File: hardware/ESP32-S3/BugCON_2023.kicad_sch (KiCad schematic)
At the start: 32 parts, among them J1 Conn_01x04_Pin, J2 Conn_01x04_Pin, J3 Conn_01x02, J4 Conn_01x01_Pin, J5 Conn_01x01_Pin, P1 USB_C_Plug_USB2.0, Q1 DMG3415U-7, SW1 RESET, SW2 GPIO, SW3 ON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

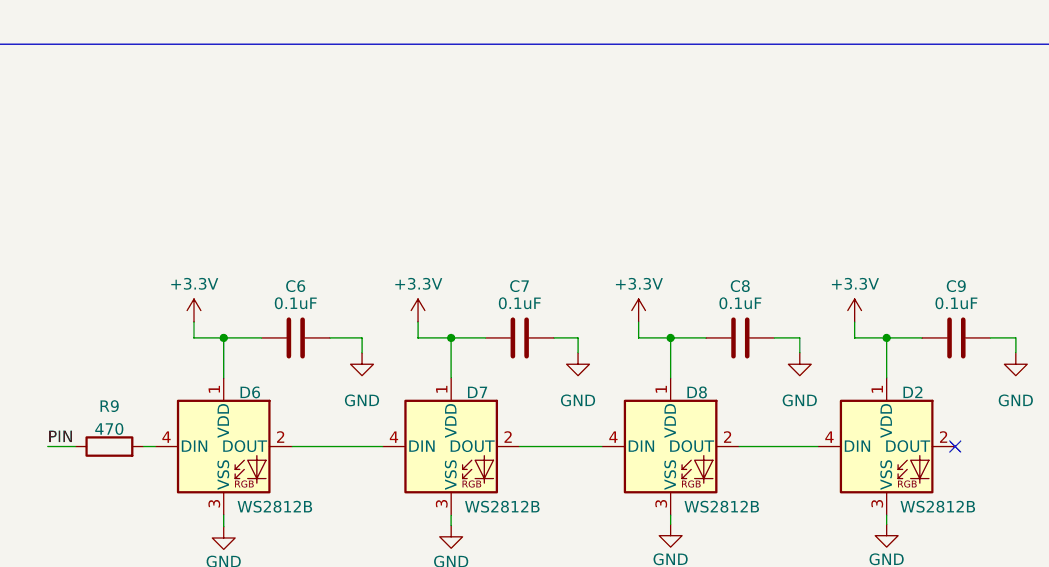
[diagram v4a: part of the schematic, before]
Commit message: fix 3.3v label on esp32 badge
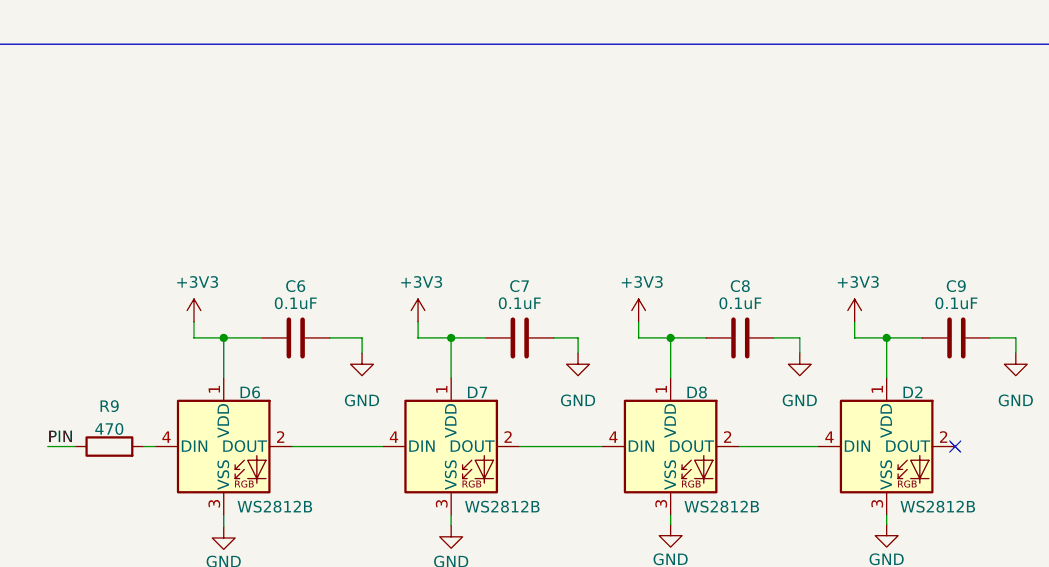
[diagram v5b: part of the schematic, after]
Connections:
- net +3.3V is gone; now on net +3V3: C6.2, C7.2, C8.2, C9.2, D2.1 (VDD), D6.1 (VDD), D7.1 (VDD), D8.1 (VDD)
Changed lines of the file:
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@@
     (effects (font (size 1.27 1.27)) (justify left bottom))
-  )
-  (symbol (lib_id "power:+3.3V") (at 231.394 121.666 0) (unit 1)
-    (in_bom yes) (on_board yes) (dnp no) (fields_autoplaced)
-    (property "Reference" "#PWR039" (at 231.394 125.476 0)
-      (effects (font (size 1.27 1.27)) hide)
-    )
-    (property "Value" "+3.3V" (at 231.394 117.475 0)
-      (effects (font (size 1.27 1.27)))
-    )
-    (property "Footprint" "" (at 231.394 121.666 0)
-      (effects (font (size 1.27 1.27)) hide)
-    )
-    (property "Datasheet" "" (at 231.394 121.666 0)
-      (effects (font (size 1.27 1.27)) hide)
-    )
-    (pin "1")
-    (instances
-      (project "BugCON_2023"
-        (path "/3bd1d1f8-54bc-46fd-8763-4ee40cf8320e"
-          (reference "#PWR039") (unit 1)
-        )
-      )
-      (project "ekoparty2023"
-        (path "/7698cad5-62ba-4b78-a0b3-4b9e419fd18c"
-          (reference "#PWR029") (unit 1)
-        )
-      )
-    )
-  )
-  (symbol (lib_id "power:+3.3V") (at 206.883 121.666 0) (unit 1)
-    (in_bom yes) (on_board yes) (dnp no) (fields_autoplaced)
-    (property "Reference" "#PWR036" (at 206.883 125.476 0)
-      (effects (font (size 1.27 1.27)) hide)
-    )
-    (property "Value" "+3.3V" (at 206.883 117.475 0)
-      (effects (font (size 1.27 1.27)))
-    )
-    (property "Footprint" "" (at 206.883 121.666 0)
-      (effects (font (size 1.27 1.27)) hide)
-    )
-    (property "Datasheet" "" (at 206.883 121.666 0)
-      (effects (font (size 1.27 1.27)) hide)
-    )
-    (pin "1")
-    (instances
-      (project "BugCON_2023"
-        (path "/3bd1d1f8-54bc-46fd-8763-4ee40cf8320e"
-          (reference "#PWR036") (unit 1)
-        )
-      )
-      (project "ekoparty2023"
-        (path "/7698cad5-62ba-4b78-a0b3-4b9e419fd18c"
-          (reference "#PWR028") (unit 1)
-        )
-      )
-    )
   )
   (symbol (lib_id "Device:C_Small") (at 106.426 37.973 0) (unit 1)
@@
     )
   )
+  (symbol (lib_id "power:+3V3") (at 206.883 121.666 0) (unit 1)
+    (in_bom yes) (on_board yes) (dnp no)
+    (property "Reference" "#PWR029" (at 206.883 125.476 0)
+      (effects (font (size 1.27 1.27)) hide)
+    )
+    (property "Value" "+3V3" (at 207.264 117.2718 0)
+      (effects (font (size 1.27 1.27)))
+    )
+    (property "Footprint" "" (at 206.883 121.666 0)
+      (effects (font (size 1.27 1.27)) hide)
+    )
+    (property "Datasheet" "" (at 206.883 121.666 0)
+      (effects (font (size 1.27 1.27)) hide)
+    )
+    (pin "1")
+    (instances
+      (project "BugCON_2023"
+        (path "/3bd1d1f8-54bc-46fd-8763-4ee40cf8320e"
+          (reference "#PWR029") (unit 1)
+        )
+      )
+      (project "minino"
+        (path "/aed8b10b-62ba-47cf-bd6c-c207f8432caa"
+          (reference "#PWR022") (unit 1)
+        )
+      )
+    )
+  )
   (symbol (lib_id "power:GND") (at 89.027 112.395 0) (unit 1)
     (in_bom yes) (on_board yes) (dnp no)
@@
     )
   )
+  (symbol (lib_id "power:+3V3") (at 255.397 121.666 0) (unit 1)
+    (in_bom yes) (on_board yes) (dnp no)
+    (property "Reference" "#PWR036" (at 255.397 125.476 0)
+      (effects (font (size 1.27 1.27)) hide)
+    )
+    (property "Value" "+3V3" (at 255.778 117.2718 0)
+      (effects (font (size 1.27 1.27)))
+    )
+    (property "Footprint" "" (at 255.397 121.666 0)
+      (effects (font (size 1.27 1.27)) hide)
+    )
+    (property "Datasheet" "" (at 255.397 121.666 0)
+      (effects (font (size 1.27 1.27)) hide)
+    )
+    (pin "1")
+    (instances
+      (project "BugCON_2023"
+        (path "/3bd1d1f8-54bc-46fd-8763-4ee40cf8320e"
+          (reference "#PWR036") (unit 1)
+        )
+      )
+      (project "minino"
+        (path "/aed8b10b-62ba-47cf-bd6c-c207f8432caa"
+          (reference "#PWR022") (unit 1)
+        )
+      )
+    )
+  )
   (symbol (lib_id "Connector:Conn_01x04_Pin") (at 24.384 116.967 0) (unit 1)
     (in_bom yes) (on_board yes) (dnp no) (fields_autoplaced)
@@
     )
   )
+  (symbol (lib_id "power:+3V3") (at 181.991 121.666 0) (unit 1)
+    (in_bom yes) (on_board yes) (dnp no)
+    (property "Reference" "#PWR032" (at 181.991 125.476 0)
+      (effects (font (size 1.27 1.27)) hide)
+    )
+    (property "Value" "+3V3" (at 182.372 117.2718 0)
+      (effects (font (size 1.27 1.27)))
+    )
+    (property "Footprint" "" (at 181.991 121.666 0)
+      (effects (font (size 1.27 1.27)) hide)
+    )
+    (property "Datasheet" "" (at 181.991 121.666 0)
+      (effects (font (size 1.27 1.27)) hide)
+    )
+    (pin "1")
+    (instances
+      (project "BugCON_2023"
+        (path "/3bd1d1f8-54bc-46fd-8763-4ee40cf8320e"
+          (reference "#PWR032") (unit 1)
+        )
+      )
+      (project "minino"
+        (path "/aed8b10b-62ba-47cf-bd6c-c207f8432caa"
+          (reference "#PWR022") (unit 1)
+        )
+      )
+    )
+  )
   (symbol (lib_id "Device:Fuse_Small") (at 47.752 21.336 0) (unit 1)
     (in_bom yes) (on_board yes) (dnp no)
@@
     )
   )
-  (symbol (lib_id "power:+3.3V") (at 181.991 121.666 0) (unit 1)
-    (in_bom yes) (on_board yes) (dnp no) (fields_autoplaced)
-    (property "Reference" "#PWR033" (at 181.991 125.476 0)
-      (effects (font (size 1.27 1.27)) hide)
-    )
-    (property "Value" "+3.3V" (at 181.991 117.475 0)
-      (effects (font (size 1.27 1.27)))
-    )
-    (property "Footprint" "" (at 181.991 121.666 0)
-      (effects (font (size 1.27 1.27)) hide)
-    )
-    (property "Datasheet" "" (at 181.991 121.666 0)
-      (effects (font (size 1.27 1.27)) hide)
-    )
-    (pin "1")
-    (instances
-      (project "BugCON_2023"
-        (path "/3bd1d1f8-54bc-46fd-8763-4ee40cf8320e"
-          (reference "#PWR033") (unit 1)
-        )
-      )
-      (project "ekoparty2023"
-        (path "/7698cad5-62ba-4b78-a0b3-4b9e419fd18c"
-          (reference "#PWR027") (unit 1)
-        )
-      )
-    )
-  )
   (symbol (lib_id "Connector_Generic:Conn_01x02") (at 38.1 85.598 0) (unit 1)
     (in_bom yes) (on_board yes) (dnp no)
@@
     )
   )
-  (symbol (lib_id "power:+3.3V") (at 255.397 121.666 0) (unit 1)
-    (in_bom yes) (on_board yes) (dnp no) (fields_autoplaced)
-    (property "Reference" "#PWR029" (at 255.397 125.476 0)
-      (effects (font (size 1.27 1.27)) hide)
-    )
-    (property "Value" "+3.3V" (at 255.397 117.475 0)
-      (effects (font (size 1.27 1.27)))
-    )
-    (property "Footprint" "" (at 255.397 121.666 0)
-      (effects (font (size 1.27 1.27)) hide)
-    )
-    (property "Datasheet" "" (at 255.397 121.666 0)
-      (effects (font (size 1.27 1.27)) hide)
-    )
-    (pin "1")
-    (instances
-      (project "BugCON_2023"
-        (path "/3bd1d1f8-54bc-46fd-8763-4ee40cf8320e"
-          (reference "#PWR029") (unit 1)
-        )
-      )
-      (project "ekoparty2023"
-        (path "/7698cad5-62ba-4b78-a0b3-4b9e419fd18c"
-          (reference "#PWR029") (unit 1)
-        )
-      )
-    )
-  )
   (symbol (lib_id "power:GND") (at 30.099 90.043 0) (unit 1)
     (in_bom yes) (on_board yes) (dnp no) (fields_autoplaced)
@@
         )
       )
+    )
+  )
+  (symbol (lib_id "power:+3V3") (at 231.394 121.666 0) (unit 1)
+    (in_bom yes) (on_board yes) (dnp no)
+    (property "Reference" "#PWR033" (at 231.394 125.476 0)
+      (effects (font (size 1.27 1.27)) hide)
+    )
+    (property "Value" "+3V3" (at 231.775 117.2718 0)
+      (effects (font (size 1.27 1.27)))
+    )
+    (property "Footprint" "" (at 231.394 121.666 0)
+      (effects (font (size 1.27 1.27)) hide)
+    )
+    (property "Datasheet" "" (at 231.394 121.666 0)
+      (effects (font (size 1.27 1.27)) hide)
+    )
+    (pin "1")
+    (instances
+      (project "BugCON_2023"
+        (path "/3bd1d1f8-54bc-46fd-8763-4ee40cf8320e"
+          (reference "#PWR033") (unit 1)
+        )
+      )
+      (project "minino"
+        (path "/aed8b10b-62ba-47cf-bd6c-c207f8432caa"
+          (reference "#PWR022") (unit 1)
+        )
+      )

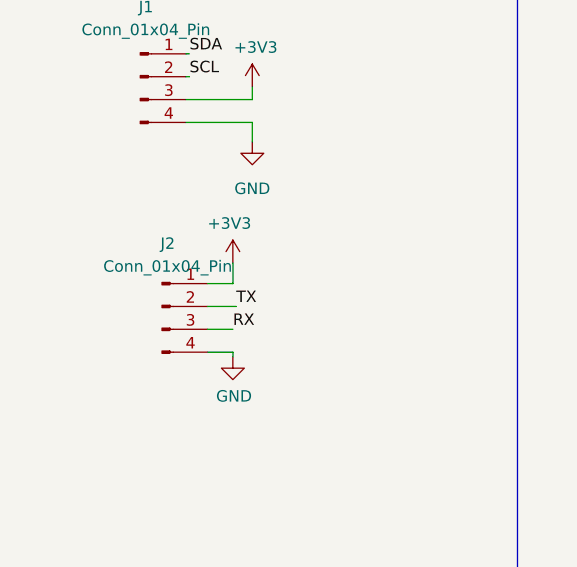
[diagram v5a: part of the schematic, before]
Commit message: remove 3.3v on Serial connector on esp32s3
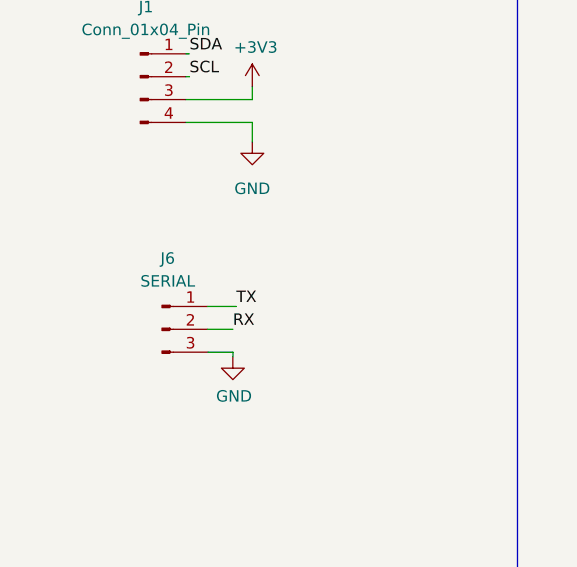
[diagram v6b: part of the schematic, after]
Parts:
- removed J2: Conn_01x04_Pin, Connector_PinSocket_2.54mm:PinSocket_1x04_P2.54mm_Vertical, symbol Connector:Conn_01x04_Pin
- added J6: SERIAL, Connector_PinSocket_2.54mm:PinSocket_1x03_P2.54mm_Vertical, symbol Connector:Conn_01x03_Pin
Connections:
- net GND: now also J6.3 (Pin_3)
- net RX: now also J6.2 (Pin_2)
- net TX: now also J6.1 (Pin_1)
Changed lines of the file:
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@@
-    (stroke (width 0) (type default))
-  )
-  (wire (pts (xy 34.671 137.668) (xy 34.671 139.954))
     (stroke (width 0) (type default))
   )
@@
   )
   (wire (pts (xy 154.305 35.052) (xy 156.337 35.052))
-    (stroke (width 0) (type default))
-  )
-  (wire (pts (xy 34.671 139.954) (xy 31.877 139.954))
     (stroke (width 0) (type default))
   )
@@
     )
   )
+  (symbol (lib_id "Connector:Conn_01x03_Pin") (at 26.797 145.034 0) (unit 1)
+    (in_bom yes) (on_board yes) (dnp no) (fields_autoplaced)
+    (property "Reference" "J6" (at 27.432 137.16 0)
+      (effects (font (size 1.27 1.27)))
+    )
+    (property "Value" "SERIAL" (at 27.432 139.7 0)
+      (effects (font (size 1.27 1.27)))
+    )
+    (property "Footprint" "Connector_PinSocket_2.54mm:PinSocket_1x03_P2.54mm_Vertical" (at 26.797 145.034 0)
+      (effects (font (size 1.27 1.27)) hide)
+    )
+    (property "Datasheet" "~" (at 26.797 145.034 0)
+      (effects (font (size 1.27 1.27)) hide)
+    )
+    (pin "1")
+    (pin "2")
+    (pin "3")
+    (instances
+      (project "BugCON_2023"
+        (path "/3bd1d1f8-54bc-46fd-8763-4ee40cf8320e"
+          (reference "J6") (unit 1)
+        )
+      )
+    )
+  )
   (symbol (lib_id "power:+3V3") (at 133.604 32.004 0) (unit 1)
     (in_bom yes) (on_board yes) (dnp no)
@@
         (path "/aed8b10b-62ba-47cf-bd6c-c207f8432caa"
           (reference "#PWR06") (unit 1)
-        )
-      )
-    )
-  )
-  (symbol (lib_id "Connector:Conn_01x04_Pin") (at 26.797 142.494 0) (unit 1)
-    (in_bom yes) (on_board yes) (dnp no) (fields_autoplaced)
-    (property "Reference" "J2" (at 27.432 135.509 0)
-      (effects (font (size 1.27 1.27)))
-    )
-    (property "Value" "Conn_01x04_Pin" (at 27.432 138.049 0)
-      (effects (font (size 1.27 1.27)))
-    )
-    (property "Footprint" "Connector_PinSocket_2.54mm:PinSocket_1x04_P2.54mm_Vertical" (at 26.797 142.494 0)
-      (effects (font (size 1.27 1.27)) hide)
-    )
-    (property "Datasheet" "~" (at 26.797 142.494 0)
-      (effects (font (size 1.27 1.27)) hide)
-    )
-    (property "Proveedor" "-- mixed values --" (at 26.797 142.494 0)
-      (effects (font (size 1.27 1.27)) hide)
-    )
-    (pin "1")
-    (pin "2")
-    (pin "3")
-    (pin "4")
-    (instances
-      (project "BugCON_2023"
-        (path "/3bd1d1f8-54bc-46fd-8763-4ee40cf8320e"
-          (reference "J2") (unit 1)
         )
       )
@@
         )
       )
-    )
-  )
-  (symbol (lib_id "power:+3V3") (at 34.671 137.668 0) (mirror y) (unit 1)
-    (in_bom yes) (on_board yes) (dnp no)
-    (property "Reference" "#PWR015" (at 34.671 141.478 0)
-      (effects (font (size 1.27 1.27)) hide)
-    )
-    (property "Value" "+3V3" (at 34.29 133.2738 0)
-      (effects (font (size 1.27 1.27)))
-    )
-    (property "Footprint" "" (at 34.671 137.668 0)
-      (effects (font (size 1.27 1.27)) hide)
-    )
-    (property "Datasheet" "" (at 34.671 137.668 0)
-      (effects (font (size 1.27 1.27)) hide)
-    )
-    (pin "1")
-    (instances
-      (project "BugCON_2023"
-        (path "/3bd1d1f8-54bc-46fd-8763-4ee40cf8320e"
-          (reference "#PWR015") (unit 1)
-        )
-      )
-      (project "minino"
-        (path "/aed8b10b-62ba-47cf-bd6c-c207f8432caa"
-          (reference "#PWR042") (unit 1)
-        )
-      )

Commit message: Change_footprint_USBC
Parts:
- P1: footprint Connector_USB:USB_C_Receptacle_G-Switch_GT-USB-7010ASV -> FootprintsB:C393939
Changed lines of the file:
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@@
       (effects (font (size 1.27 1.27)))
     )
-    (property "Footprint" "Connector_USB:USB_C_Receptacle_G-Switch_GT-USB-7010ASV" (at 30.734 36.576 0)
+    (property "Footprint" "FootprintsB:C393939" (at 30.734 36.576 0)
       (effects (font (size 1.27 1.27)) hide)
     )

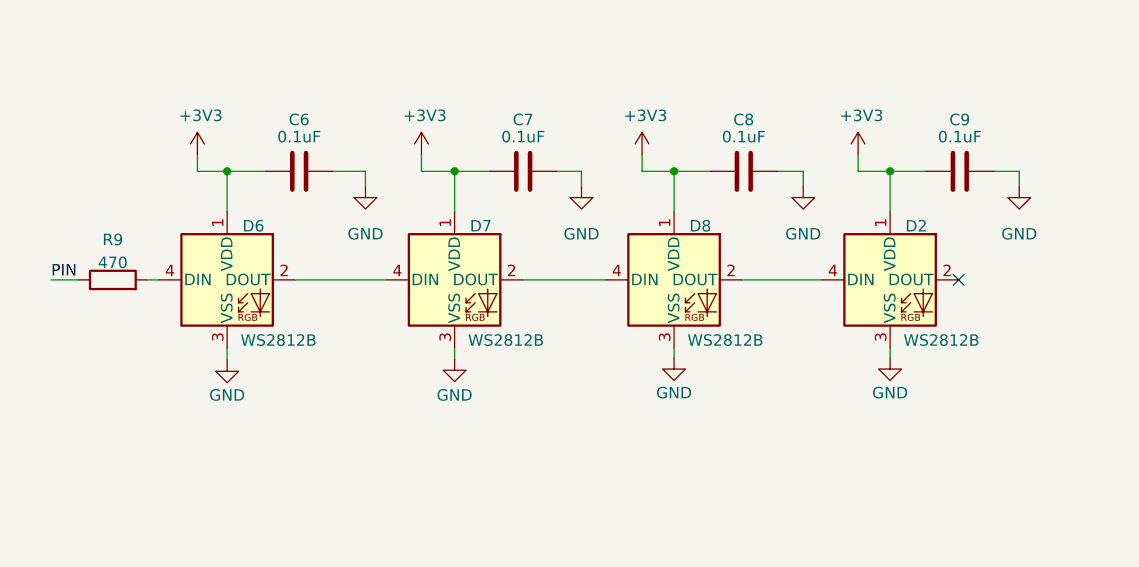
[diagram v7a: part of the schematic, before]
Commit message: Change_LED´s_Change_Touch_Pad
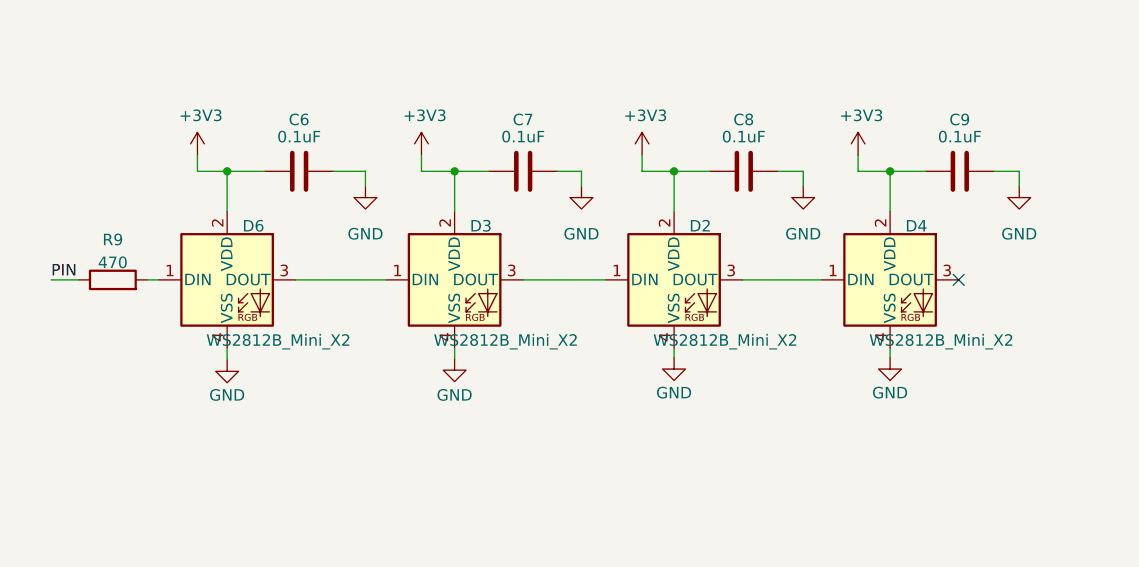
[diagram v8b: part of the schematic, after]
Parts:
- removed D7, D8: WS2812B, FootprintsB:LED_SK6812MINI_PLCC4_3.5x3.5mm_P1.75mm, symbol LED:WS2812B
- added D3, D4: WS2812B_Mini_X2, FootprintsB:LED-SMD_4P-L3.5-W3.5-TL_WS2812B-1, symbol LED:WS2812B
- D2, D6: value WS2812B -> WS2812B_Mini_X2; footprint FootprintsB:LED_SK6812MINI_PLCC4_3.5x3.5mm_P1.75mm -> FootprintsB:LED-SMD_4P-L3.5-W3.5-TL_WS2812B-1; LCSC# C527089 -> C4154873; manf# WS2812B-Mini -> WS2812B-Mini-x2
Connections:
- net +3V3: now also D2.2 (VDD), D6.2 (VDD), D3.2 (VDD), D4.2 (VDD); no longer D2.1 (VDD), D6.1 (VDD)
- net GND: now also D2.4 (VSS), D6.4 (VSS), D3.4 (VSS), D4.4 (VSS); no longer D2.3 (VSS), D6.3 (VSS)
- net at R9.2: now also D6.1 (DIN); no longer D6.4 (DIN)
- new net: D2.3 (DOUT), D4.1 (DIN)
- new net: D2.1 (DIN), D3.3 (DOUT)
- new net: D3.1 (DIN), D6.3 (DOUT)
